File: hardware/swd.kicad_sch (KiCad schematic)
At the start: 3 parts, among them IC4 ESDALC6V1W5, J2 22-16-2060

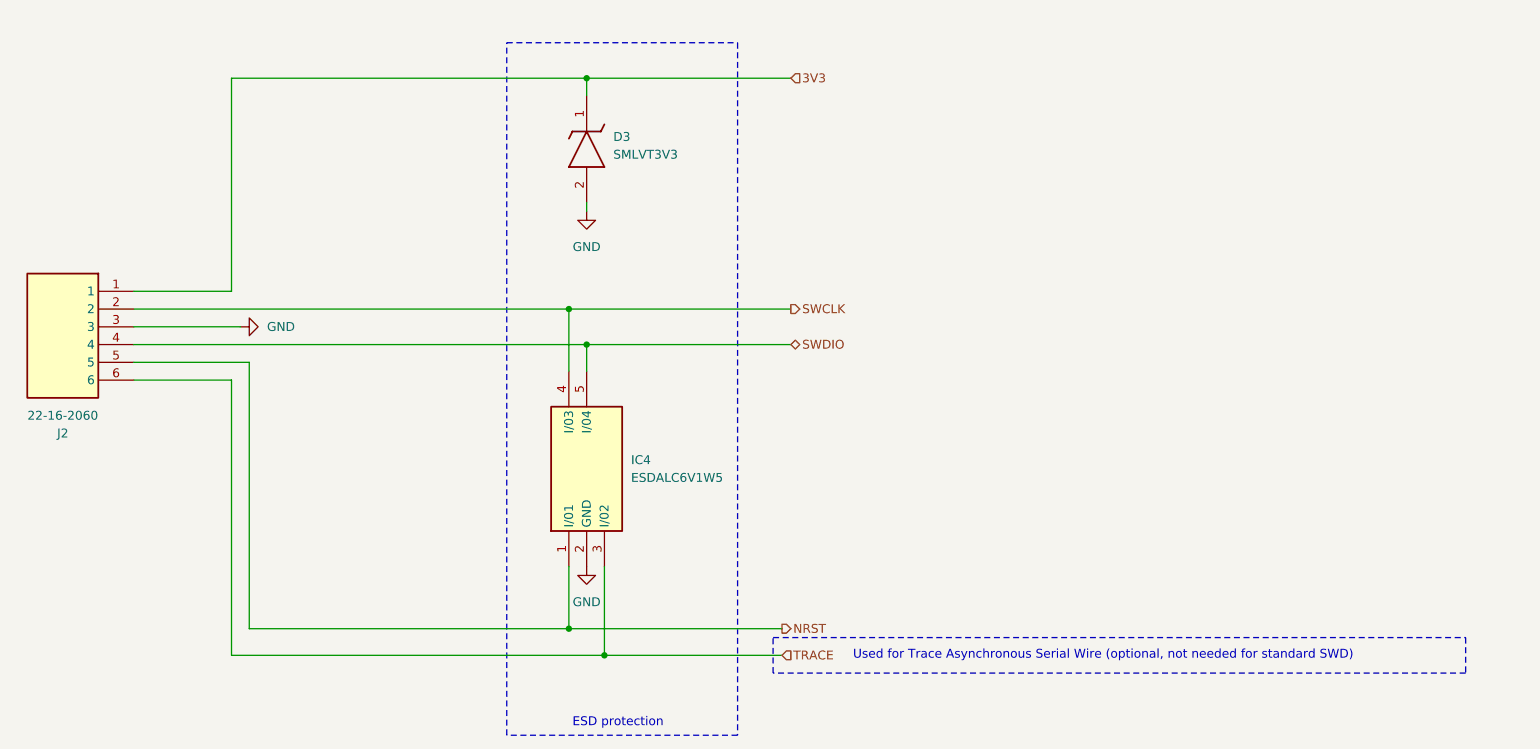
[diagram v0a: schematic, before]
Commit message: Battery temperature meter added to MCU
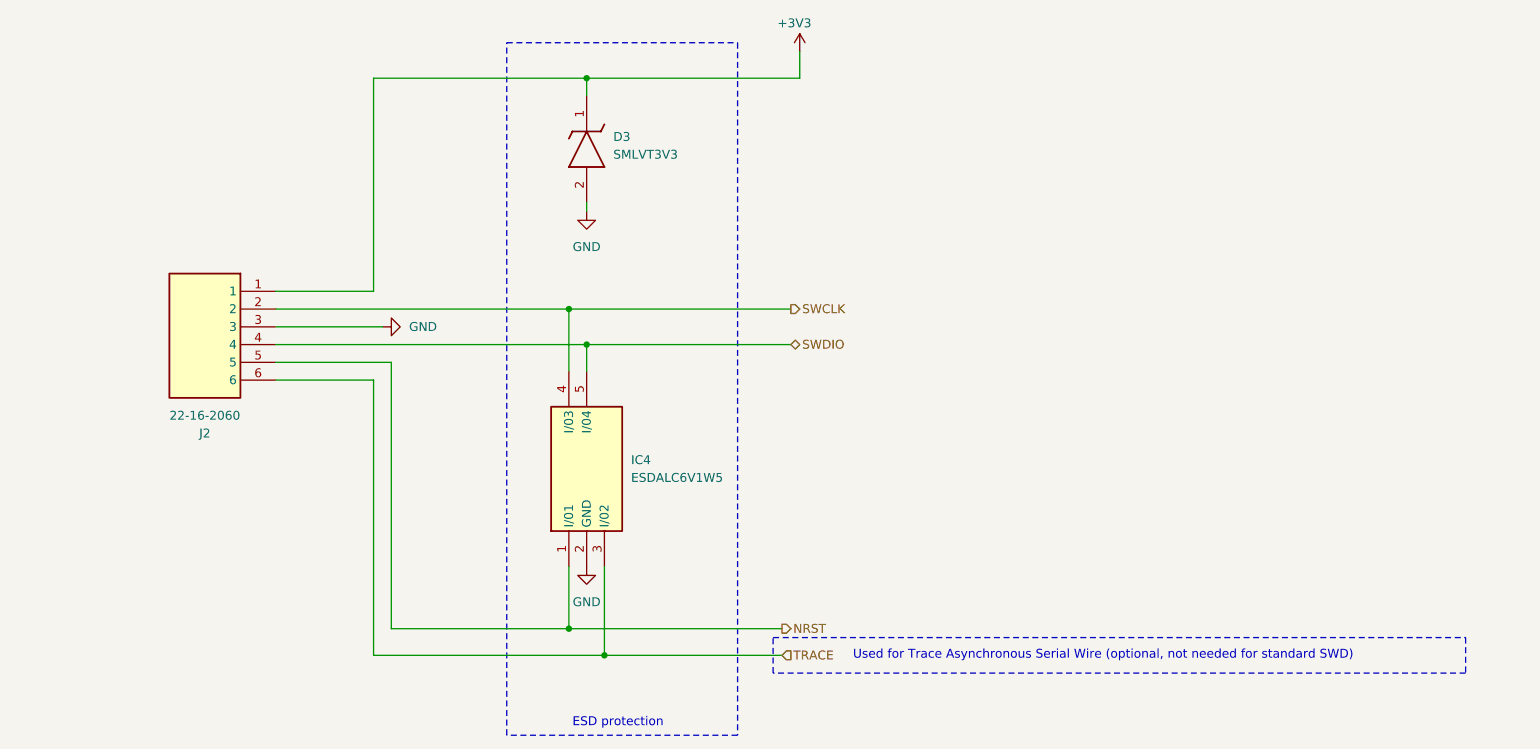
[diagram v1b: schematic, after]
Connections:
- net 3V3 renamed +3V3
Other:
- moved on the sheet: J2
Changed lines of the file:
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@@
+	(wire
+		(pts
+			(xy 170.18 30.48) (xy 170.18 34.29)
+		)
+		(stroke
+			(width 0)
+			(type default)
+		)
+	)
 	(wire
 		(pts
@@
 	(wire
 		(pts
-			(xy 74.93 67.31) (xy 137.16 67.31)
+			(xy 95.25 67.31) (xy 137.16 67.31)
 		)
 		(stroke
@@
 	(wire
 		(pts
-			(xy 88.9 77.47) (xy 74.93 77.47)
+			(xy 109.22 77.47) (xy 95.25 77.47)
 		)
 		(stroke
@@
 	(wire
 		(pts
-			(xy 88.9 116.84) (xy 142.24 116.84)
+			(xy 109.22 116.84) (xy 142.24 116.84)
 		)
 		(stroke
@@
 	(wire
 		(pts
-			(xy 91.44 74.93) (xy 91.44 113.03)
-		)
-		(stroke
-			(width 0)
-			(type default)
-		)
-	)
-	(wire
-		(pts
-			(xy 88.9 116.84) (xy 88.9 77.47)
-		)
-		(stroke
-			(width 0)
-			(type default)
-		)
-	)
-	(wire
-		(pts
-			(xy 88.9 34.29) (xy 139.7 34.29)
-		)
-		(stroke
-			(width 0)
-			(type default)
-		)
-	)
-	(wire
-		(pts
-			(xy 139.7 34.29) (xy 168.91 34.29)
-		)
-		(stroke
-			(width 0)
-			(type default)
-		)
-	)
-	(wire
-		(pts
-			(xy 74.93 74.93) (xy 91.44 74.93)
+			(xy 111.76 74.93) (xy 111.76 113.03)
+		)
+		(stroke
+			(width 0)
+			(type default)
+		)
+	)
+	(wire
+		(pts
+			(xy 109.22 116.84) (xy 109.22 77.47)
+		)
+		(stroke
+			(width 0)
+			(type default)
+		)
+	)
+	(wire
+		(pts
+			(xy 109.22 34.29) (xy 139.7 34.29)
+		)
+		(stroke
+			(width 0)
+			(type default)
+		)
+	)
+	(wire
+		(pts
+			(xy 139.7 34.29) (xy 170.18 34.29)
+		)
+		(stroke
+			(width 0)
+			(type default)
+		)
+	)
+	(wire
+		(pts
+			(xy 95.25 74.93) (xy 111.76 74.93)
 		)
 		(stroke
@@
 	(wire
 		(pts
-			(xy 74.93 64.77) (xy 88.9 64.77)
+			(xy 95.25 64.77) (xy 109.22 64.77)
 		)
 		(stroke
@@
 	(wire
 		(pts
-			(xy 74.93 69.85) (xy 90.17 69.85)
-		)
-		(stroke
-			(width 0)
-			(type default)
-		)
-	)
-	(wire
-		(pts
-			(xy 91.44 113.03) (xy 137.16 113.03)
-		)
-		(stroke
-			(width 0)
-			(type default)
-		)
-	)
-	(wire
-		(pts
-			(xy 74.93 72.39) (xy 139.7 72.39)
-		)
-		(stroke
-			(width 0)
-			(type default)
-		)
-	)
-	(wire
-		(pts
-			(xy 88.9 64.77) (xy 88.9 34.29)
+			(xy 95.25 69.85) (xy 110.49 69.85)
+		)
+		(stroke
+			(width 0)
+			(type default)
+		)
+	)
+	(wire
+		(pts
+			(xy 111.76 113.03) (xy 137.16 113.03)
+		)
+		(stroke
+			(width 0)
+			(type default)
+		)
+	)
+	(wire
+		(pts
+			(xy 95.25 72.39) (xy 139.7 72.39)
+		)
+		(stroke
+			(width 0)
+			(type default)
+		)
+	)
+	(wire
+		(pts
+			(xy 109.22 64.77) (xy 109.22 34.29)
 		)
 		(stroke
@@
 		(shape output)
 		(at 168.91 67.31 0)
-		(effects
-			(font
-				(size 1.27 1.27)
-			)
-			(justify left)
-		)
-	)
-	(hierarchical_label "3V3"
-		(shape input)
-		(at 168.91 34.29 0)
 		(effects
 			(font
@@
 	(symbol
 		(lib_id "SamacSys_Parts:22-16-2060")
-		(at 74.93 64.77 0)
+		(at 95.25 64.77 0)
 		(mirror y)
 		(unit 1)
@@
 		(dnp no)
 		(property "Reference" "J2"
-			(at 64.77 85.09 0)
+			(at 85.09 85.09 0)
 			(effects
 				(font
@@
 		)
 		(property "Value" "22-16-2060"
-			(at 64.77 82.55 0)
+			(at 85.09 82.55 0)
 			(effects
 				(font
@@
 		)
 		(property "Footprint" "22162060"
-			(at 58.42 159.69 0)
+			(at 78.74 159.69 0)
 			(effects
 				(font
@@
 		)
 		(property "Datasheet" "https://www.molex.com/content/dam/molex/molex-dot-com/products/automated/en-us/salesdrawingpdf/445/4455/022162060_sd.pdf?inline"
-			(at 58.42 259.69 0)
+			(at 78.74 259.69 0)
 			(effects
 				(font
@@
 		)
 		(property "Description" "CONNECTOR, RCPT, 6POS, 2.54MM"
-			(at 74.93 64.77 0)
+			(at 95.25 64.77 0)
 			(effects
 				(font
@@
 		)
 		(property "Height" "8.71"
-			(at 58.42 459.69 0)
+			(at 78.74 459.69 0)
 			(effects
 				(font
@@
 		)
 		(property "Manufacturer_Name" "Molex"
-			(at 58.42 559.69 0)
+			(at 78.74 559.69 0)
 			(effects
 				(font
@@
 		)
 		(property "Manufacturer_Part_Number" "22-16-2060"
-			(at 58.42 659.69 0)
+			(at 78.74 659.69 0)
 			(effects
 				(font
@@
 		)
 		(property "Mouser Part Number" "538-22-16-2060"
-			(at 58.42 759.69 0)
+			(at 78.74 759.69 0)
 			(effects
 				(font
@@
 		)
 		(property "Mouser Price/Stock" "https://www.mouser.com/Search/Refine.aspx?Keyword=538-22-16-2060"
-			(at 58.42 859.69 0)
+			(at 78.74 859.69 0)
 			(effects
 				(font
@@
 		)
 		(property "Arrow Part Number" ""
-			(at 58.42 959.69 0)
+			(at 78.74 959.69 0)
 			(effects
 				(font
@@
 		)
 		(property "Arrow Price/Stock" ""
-			(at 58.42 1059.69 0)
+			(at 78.74 1059.69 0)
 			(effects
 				(font
@@
 	(symbol
 		(lib_id "power:GND")
-		(at 90.17 69.85 90)
+		(at 110.49 69.85 90)
 		(unit 1)
 		(exclude_from_sim no)
@@
 		(fields_autoplaced yes)
 		(property "Reference" "#PWR013"
-			(at 96.52 69.85 0)
+			(at 116.84 69.85 0)
 			(effects
 				(font
@@
 		)
 		(property "Value" "GND"
-			(at 93.98 69.8499 90)
+			(at 114.3 69.8499 90)
 			(effects
 				(font
@@
 		)
 		(property "Footprint" ""
-			(at 90.17 69.85 0)
+			(at 110.49 69.85 0)
 			(effects
 				(font
@@
 		)
 		(property "Datasheet" ""
-			(at 90.17 69.85 0)
+			(at 110.49 69.85 0)
 			(effects
 				(font
@@
 		)
 		(property "Description" "Power symbol creates a global label with name \"GND\" , ground"
-			(at 90.17 69.85 0)
+			(at 110.49 69.85 0)
 			(effects
 				(font
@@
 					(unit 1)
 				)
+			)
+		)
+	)
+	(symbol
+		(lib_id "power:+3V3")
+		(at 170.18 30.48 0)
+		(unit 1)
+		(exclude_from_sim no)
+		(in_bom yes)
+		(on_board yes)
+		(dnp no)
+		(property "Reference" "#PWR069"
+			(at 170.18 34.29 0)
+			(effects
+				(font
+					(size 1.27 1.27)
+				)
+				(hide yes)
+			)
+		)
+		(property "Value" "+3V3"
+			(at 169.418 26.416 0)
+			(effects
+				(font
+					(size 1.27 1.27)
+				)
+			)
+		)
+		(property "Footprint" ""
+			(at 170.18 30.48 0)
+			(effects
+				(font
+					(size 1.27 1.27)
+				)
+				(hide yes)
+			)
+		)
+		(property "Datasheet" ""
+			(at 170.18 30.48 0)
+			(effects
+				(font
+					(size 1.27 1.27)
+				)
+				(hide yes)
+			)
+		)
+		(property "Description" "Power symbol creates a global label with name \"+3V3\""
+			(at 170.18 30.48 0)
+			(effects
+				(font
+					(size 1.27 1.27)
+				)
+				(hide yes)
+			)
+		)
+		(pin "1"
+		)
+		(instances
+			(project "obvod"
+				(path "/e8e834c4-1afb-42f7-b718-3cb720dae1d5/d3fe727f-e59c-4b25-a97d-baf79ecd8dec"
+					(reference "#PWR069")
+					(unit 1)
+				)

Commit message: Revised and completed BOM
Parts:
- renumbered D3 to D5, IC4 to IC6
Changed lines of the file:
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@@
 		(dnp no)
 		(fields_autoplaced yes)
-		(property "Reference" "IC4"
+		(property "Reference" "IC6"
 			(at 146.05 88.8999 90)
 			(effects
@@
 			(project "obvod"
 				(path "/e8e834c4-1afb-42f7-b718-3cb720dae1d5/d3fe727f-e59c-4b25-a97d-baf79ecd8dec"
-					(reference "IC4")
+					(reference "IC6")
 					(unit 1)
 				)
@@
 		(dnp no)
 		(fields_autoplaced yes)
-		(property "Reference" "D3"
+		(property "Reference" "D5"
 			(at 143.51 42.6719 90)
 			(effects
@@
 			(project "obvod"
 				(path "/e8e834c4-1afb-42f7-b718-3cb720dae1d5/d3fe727f-e59c-4b25-a97d-baf79ecd8dec"
-					(reference "D3")
+					(reference "D5")
 					(unit 1)
 				)
